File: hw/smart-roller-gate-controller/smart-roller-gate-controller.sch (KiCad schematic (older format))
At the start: 37 parts

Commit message: hw: sch complete, alpha version
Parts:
- R? (x2): value 10k -> 4.7k
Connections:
- net SCL is gone; now on net PZ_TX: DD?.36 (IO22)
- net SDA is gone; now on net PZ_RX: DD?.33 (IO21)
- net BLK1: now also DD?.12 (IO27)
- net BLK2: now also DD?.8 (IO32)
- net D_BUSY: now also DD?.6 (IO34)
- net D_DIN: now also DD?.16 (IO13); no longer DD?.14 (IO12)
- net GND: now also XP?.3 (Pin_3)
- net S2_ISR: now also DD?.7 (IO35)
- net ~RSNS: now also DD?.9 (IO33)
- net ~S2_RST: now also DD?.11 (IO26)
- net MOSI renamed MISO
- net MISO: now also DD?.14 (IO12); no longer DD?.16 (IO13)
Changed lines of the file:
@@
 Text GLabel 3800 2850 2    50   Output ~ 0
 ~RESET
-Text GLabel 3600 4250 2    50   Output ~ 0
+Text GLabel 3600 4250 2    50   UnSpc ~ 0
 ~RSNS
 Text GLabel 5050 2600 0    50   Input ~ 0
 ~RESET
-Text Notes 11300 7350 0    50   ~ 0
+Text Notes 11650 8650 0    50   ~ 0
 According to datasheet it is not necessary to pull-up/pull-down pins\n\nhttps://www.espressif.com/sites/default/files/documentation/esp32-wroom-32d_esp32-wroom-32u_datasheet_en.pdf
 $Comp
@@
 Wire Wire Line
 	13550 3850 13950 3850
+Text GLabel 13950 3750 2    50   Input ~ 0
+MISO
 Text GLabel 12400 3650 0    50   Input ~ 0
-MISO
-Text GLabel 13950 3750 2    50   Input ~ 0
 MOSI
 Text GLabel 13950 3650 2    50   Input ~ 0
@@
 P 5650 9300
 F 0 "R?" H 5720 9346 50  0000 L CNN
-F 1 "10k" H 5720 9255 50  0000 L CNN
+F 1 "4.7k" H 5720 9255 50  0000 L CNN
 F 2 "" V 5580 9300 50  0001 C CNN
 F 3 "~" H 5650 9300 50  0001 C CNN
@@
 P 5650 9400
 F 0 "R?" H 5720 9446 50  0000 L CNN
-F 1 "10k" H 5720 9355 50  0000 L CNN
+F 1 "4.7k" H 5720 9355 50  0000 L CNN
 F 2 "" V 5580 9400 50  0001 C CNN
 F 3 "~" H 5650 9400 50  0001 C CNN
@@
 Wire Wire Line
 	12500 2850 12400 2850
-Text GLabel 8850 6050 2    50   Input ~ 0
+Text GLabel 7600 4000 2    50   Output ~ 0
 PZ_RX
-Text GLabel 8900 6200 2    50   Output ~ 0
+Text GLabel 7600 4100 2    50   Input ~ 0
 PZ_TX
-Text GLabel 7600 4100 2    50   Input ~ 0
-SCL
-Text GLabel 7600 4000 2    50   Input ~ 0
-SDA
+Text GLabel 7600 4400 2    50   Input ~ 0
+~S2_RST
+Wire Wire Line
+	7000 4400 7600 4400
+Text GLabel 7150 4500 2    50   UnSpc ~ 0
+BLK1
+Text GLabel 7150 4600 2    50   UnSpc ~ 0
+BLK2
+Wire Wire Line
+	7000 4600 7150 4600
+Wire Wire Line
+	7150 4700 7000 4700
+Text GLabel 7150 4700 2    50   UnSpc ~ 0
+~RSNS
+Wire Wire Line
+	7000 4500 7150 4500
+Text GLabel 7550 4800 2    50   Input ~ 0
+D_BUSY
+Text GLabel 7550 4900 2    50   Input ~ 0
+S2_ISR
+Wire Wire Line
+	7000 4800 7550 4800
+Wire Wire Line
+	7000 4900 7550 4900
+Wire Wire Line
+	2900 4350 3200 4350
+Wire Wire Line
+	3200 4350 3200 4450
+Connection ~ 3200 4450
 $EndSCHEMATC

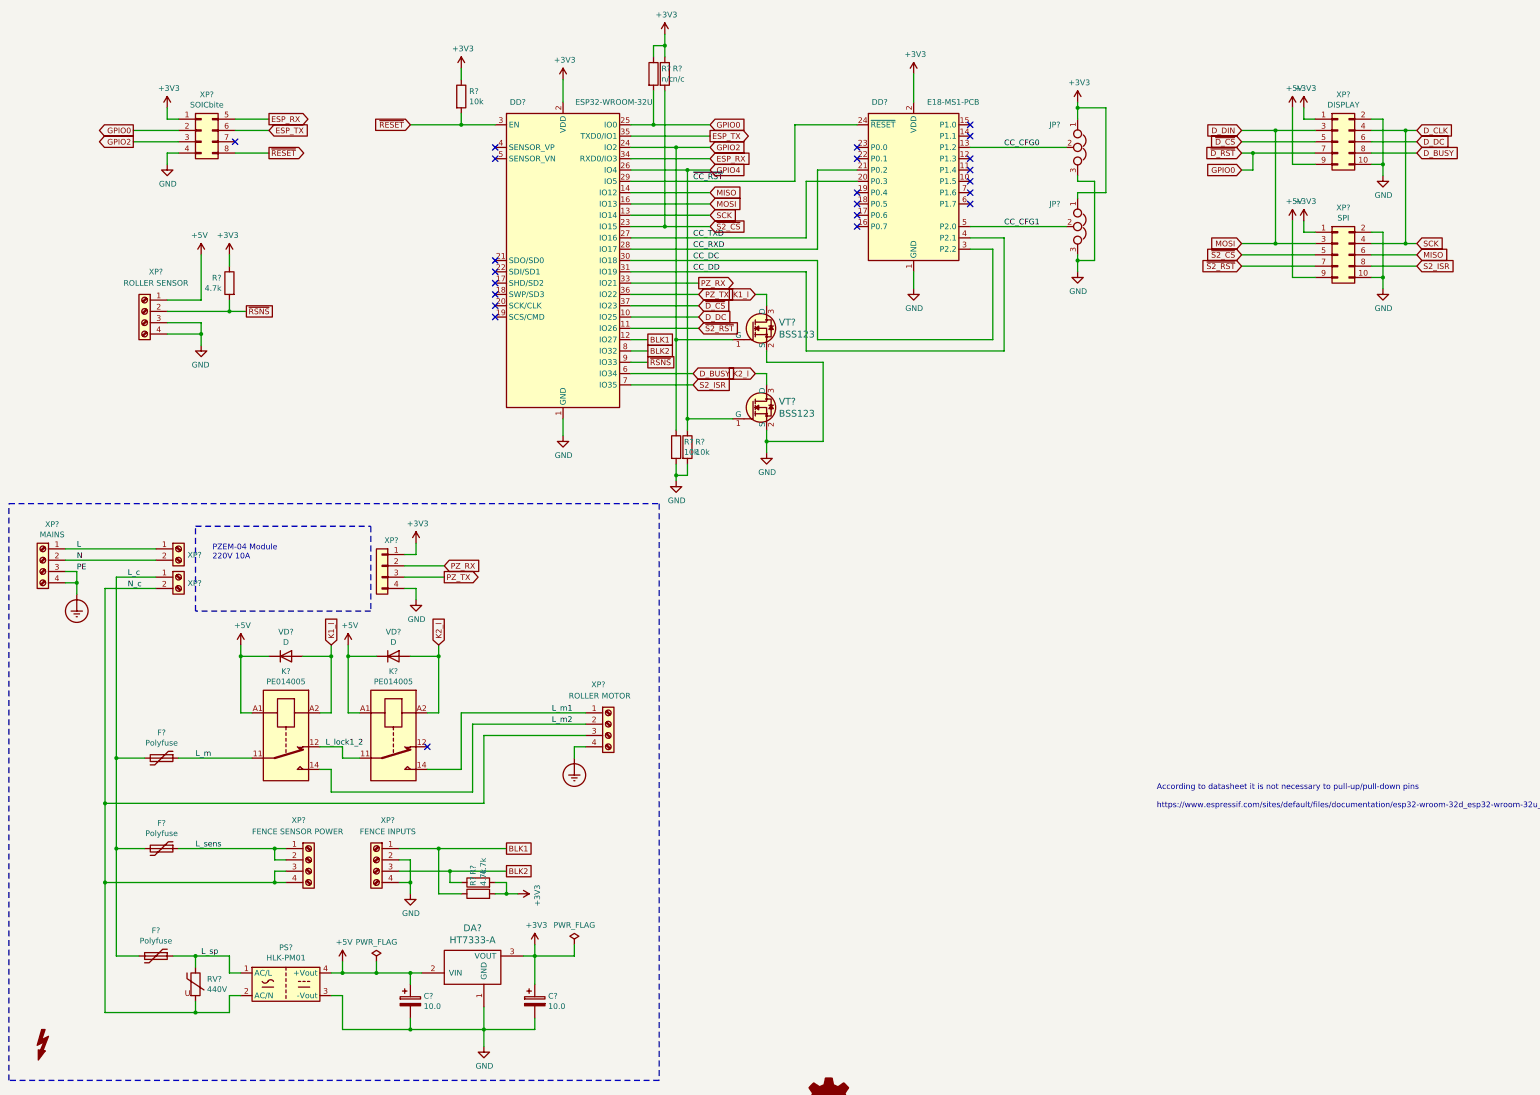
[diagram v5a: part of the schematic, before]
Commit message: hw: optimize pinout a bit
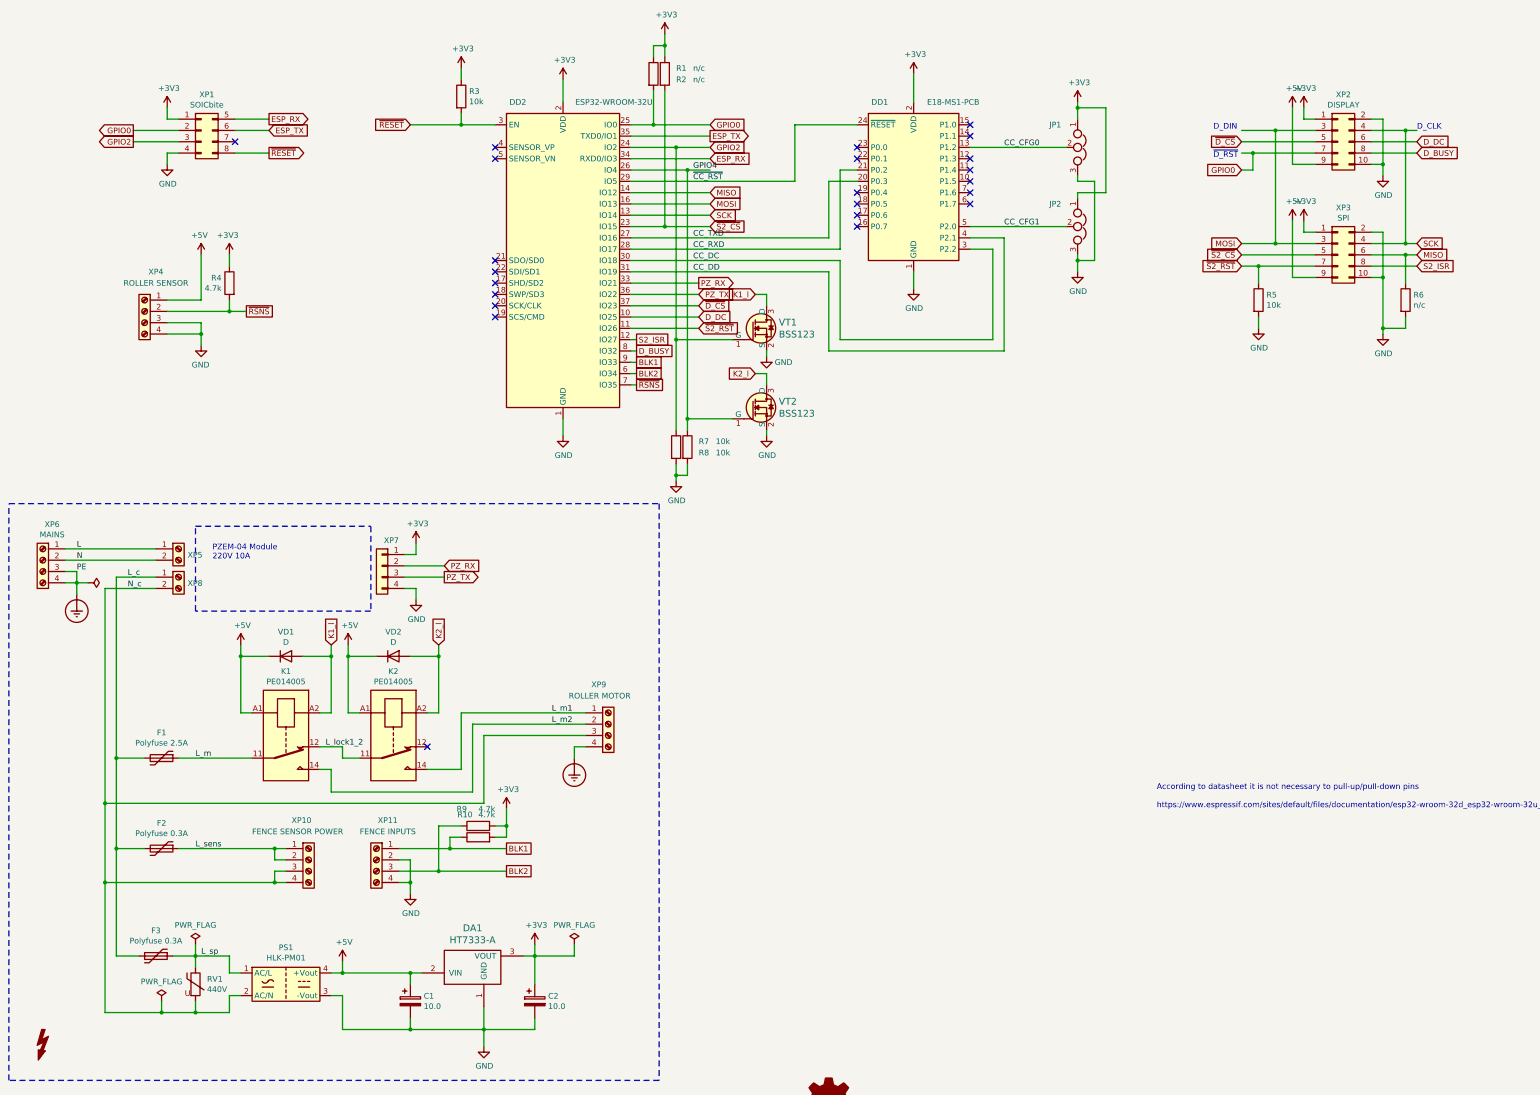
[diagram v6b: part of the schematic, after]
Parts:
- added R5: 10k, symbol Device:R
- added R6: n/c, symbol Device:R
- DA1: renamed from DA?; footprint (none) -> Package_TO_SOT_SMD:SOT-89-3
- F1: renamed from F?; value Polyfuse -> Polyfuse 2.5A
- F2, F3: renamed from F?; value Polyfuse -> Polyfuse 0.3A
- gave numbers to parts that had none: 33
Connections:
- net BLK1: now also DD2.9 (IO33); no longer DD2.12 (IO27)
- net BLK2: now also DD2.6 (IO34); no longer DD2.8 (IO32)
- net D_BUSY: now also DD2.8 (IO32); no longer DD2.6 (IO34)
- net GND: now also R5.2, R6.2
- net MISO: now also R6.1
- net S2_ISR: now also DD2.12 (IO27); no longer DD2.7 (IO35)
- net ~RSNS: now also DD2.7 (IO35); no longer DD2.9 (IO33)
- net ~S2_RST: now also R5.1
- net D_CLK renamed SCK
- net D_DIN renamed MOSI
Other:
- note added: "D_CLK"
- note added: "D_DIN"
- note added: "~D_RST"
- moved on the sheet: R10, R9

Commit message: hw: start routing
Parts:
- F1: footprint (none) -> Fuse:Fuse_Bourns_MF-RHT1300
- F2, F3: footprint (none) -> Fuse:Fuse_Bourns_MF-RHT200
- JP1, JP2: footprint (none) -> Jumper:SolderJumper-3_P1.3mm_Open_RoundedPad1.0x1.5mm
- R1, R10, R2, R3, R4, R5, R6, R7, R8, R9: footprint (none) -> Resistor_SMD:R_0603_1608Metric_Pad1.05x0.95mm_HandSolder
- RV1: footprint (none) -> Varistor:RV_Disc_D21.5mm_W4.9mm_P10mm
- VD1, VD2: footprint (none) -> Diode_SMD:D_SOD-123
- XP10, XP11, XP4, XP6, XP9: footprint (none) -> smart-roller-gate-controller:CONN-KF250-BA-4
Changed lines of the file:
@@
 F 0 "F3" V 2575 9950 50  0000 C CNN
 F 1 "Polyfuse 0.3A" V 2666 9950 50  0000 C CNN
-F 2 "" H 2850 9750 50  0001 L CNN
+F 2 "Fuse:Fuse_Bourns_MF-RHT200" H 2850 9750 50  0001 L CNN
 F 3 "~" H 2800 9950 50  0001 C CNN
 	1    2800 9950
@@
 F 0 "JP1" V 10750 2550 50  0000 L CNN
 F 1 "Jumper_NC_Dual" V 10995 2902 50  0001 L CNN
-F 2 "" H 10950 2800 50  0001 C CNN
+F 2 "Jumper:SolderJumper-3_P1.3mm_Open_RoundedPad1.0x1.5mm" H 10950 2800 50  0001 C CNN
 F 3 "~" H 10950 2800 50  0001 C CNN
 	1    10950 2800
@@
 F 0 "JP2" V 10750 3250 50  0000 L CNN
 F 1 "Jumper_NC_Dual" V 11050 3800 50  0001 L CNN
-F 2 "" H 10950 3500 50  0001 C CNN
+F 2 "Jumper:SolderJumper-3_P1.3mm_Open_RoundedPad1.0x1.5mm" H 10950 3500 50  0001 C CNN
 F 3 "~" H 10950 3500 50  0001 C CNN
 	1    10950 3500
@@
 F 0 "RV1" H 3252 10246 50  0000 L CNN
 F 1 "440V" H 3252 10155 50  0000 L CNN
-F 2 "" V 3080 10200 50  0001 C CNN
+F 2 "Varistor:RV_Disc_D21.5mm_W4.9mm_P10mm" V 3080 10200 50  0001 C CNN
 F 3 "~" H 3150 10200 50  0001 C CNN
 	1    3150 10200
@@
 F 0 "XP6" H 1718 6767 50  0000 C CNN
 F 1 "MAINS" H 1718 6676 50  0000 C CNN
-F 2 "" H 1800 6450 50  0001 C CNN
+F 2 "smart-roller-gate-controller:CONN-KF250-BA-4" H 1800 6450 50  0001 C CNN
 F 3 "~" H 1800 6450 50  0001 C CNN
 	1    1800 6450
@@
 F 0 "F2" V 2625 9000 50  0000 C CNN
 F 1 "Polyfuse 0.3A" V 2716 9000 50  0000 C CNN
-F 2 "" H 2900 8800 50  0001 L CNN
+F 2 "Fuse:Fuse_Bourns_MF-RHT200" H 2900 8800 50  0001 L CNN
 F 3 "~" H 2850 9000 50  0001 C CNN
 	1    2850 9000
@@
 F 0 "XP10" H 4000 9450 50  0000 L CNN
 F 1 "FENCE SENSOR POWER" H 3650 9350 50  0000 L CNN
-F 2 "" H 4150 9100 50  0001 C CNN
+F 2 "smart-roller-gate-controller:CONN-KF250-BA-4" H 4150 9100 50  0001 C CNN
 F 3 "~" H 4150 9100 50  0001 C CNN
 	1    4150 9100
@@
 F 0 "XP9" H 6650 8250 50  0000 L CNN
 F 1 "ROLLER MOTOR" H 6450 8150 50  0000 L CNN
-F 2 "" H 6800 7900 50  0001 C CNN
+F 2 "smart-roller-gate-controller:CONN-KF250-BA-4" H 6800 7900 50  0001 C CNN
 F 3 "~" H 6800 7900 50  0001 C CNN
 	1    6800 7900
@@
 F 0 "XP11" H 4650 9450 50  0000 C CNN
 F 1 "FENCE INPUTS" H 4650 9350 50  0000 C CNN
-F 2 "" H 4750 9100 50  0001 C CNN
+F 2 "smart-roller-gate-controller:CONN-KF250-BA-4" H 4750 9100 50  0001 C CNN
 F 3 "~" H 4750 9100 50  0001 C CNN
 	1    4750 9100
@@
 F 0 "XP4" H 2600 4600 50  0000 C CNN
 F 1 "ROLLER SENSOR" H 2600 4500 50  0000 C CNN
-F 2 "" H 2700 4250 50  0001 C CNN
+F 2 "smart-roller-gate-controller:CONN-KF250-BA-4" H 2700 4250 50  0001 C CNN
 F 3 "~" H 2700 4250 50  0001 C CNN
 	1    2700 4250
@@
 F 0 "R3" H 5570 2396 50  0000 L CNN
 F 1 "10k" H 5570 2305 50  0000 L CNN
-F 2 "" V 5430 2350 50  0001 C CNN
+F 2 "Resistor_SMD:R_0603_1608Metric_Pad1.05x0.95mm_HandSolder" V 5430 2350 50  0001 C CNN
 F 3 "~" H 5500 2350 50  0001 C CNN
 	1    5500 2350
@@
 F 0 "F1" V 2625 8200 50  0000 C CNN
 F 1 "Polyfuse 2.5A" V 2716 8200 50  0000 C CNN
-F 2 "" H 2900 8000 50  0001 L CNN
+F 2 "Fuse:Fuse_Bourns_MF-RHT1300" H 2900 8000 50  0001 L CNN
 F 3 "~" H 2850 8200 50  0001 C CNN
 	1    2850 8200
@@
 F 0 "VD1" H 3950 7516 50  0000 C CNN
 F 1 "D" H 3950 7425 50  0000 C CNN
-F 2 "" H 3950 7300 50  0001 C CNN
+F 2 "Diode_SMD:D_SOD-123" H 3950 7300 50  0001 C CNN
 F 3 "~" H 3950 7300 50  0001 C CNN
 	1    3950 7300
@@
 F 0 "VD2" H 4900 7516 50  0000 C CNN
 F 1 "D" H 4900 7425 50  0000 C CNN
-F 2 "" H 4900 7300 50  0001 C CNN
+F 2 "Diode_SMD:D_SOD-123" H 4900 7300 50  0001 C CNN
 F 3 "~" H 4900 7300 50  0001 C CNN
 	1    4900 7300
@@
 F 0 "R4" H 3520 4046 50  0000 L CNN
 F 1 "4.7k" H 3520 3955 50  0000 L CNN
-F 2 "" V 3380 4000 50  0001 C CNN
+F 2 "Resistor_SMD:R_0603_1608Metric_Pad1.05x0.95mm_HandSolder" V 3380 4000 50  0001 C CNN
 F 3 "~" H 3450 4000 50  0001 C CNN
 	1    3450 4000
@@
 F 0 "R1" H 7400 2200 50  0000 L CNN
 F 1 "n/c" H 7550 2200 50  0000 L CNN
-F 2 "" V 7130 2150 50  0001 C CNN
+F 2 "Resistor_SMD:R_0603_1608Metric_Pad1.05x0.95mm_HandSolder" V 7130 2150 50  0001 C CNN
 F 3 "~" H 7200 2150 50  0001 C CNN
 	1    7200 2150
@@
 F 0 "R2" H 7400 2100 50  0000 L CNN
 F 1 "n/c" H 7550 2100 50  0000 L CNN
-F 2 "" V 7230 2150 50  0001 C CNN
+F 2 "Resistor_SMD:R_0603_1608Metric_Pad1.05x0.95mm_HandSolder" V 7230 2150 50  0001 C CNN
 F 3 "~" H 7300 2150 50  0001 C CNN
 	1    7300 2150
@@
 F 0 "R7" H 7600 5500 50  0000 L CNN
 F 1 "10k" H 7750 5500 50  0000 L CNN
-F 2 "" V 7330 5450 50  0001 C CNN
+F 2 "Resistor_SMD:R_0603_1608Metric_Pad1.05x0.95mm_HandSolder" V 7330 5450 50  0001 C CNN
 F 3 "~" H 7400 5450 50  0001 C CNN
 	1    7400 5450
@@
 F 0 "R8" H 7600 5400 50  0000 L CNN
 F 1 "10k" H 7750 5400 50  0000 L CNN
-F 2 "" V 7430 5450 50  0001 C CNN
+F 2 "Resistor_SMD:R_0603_1608Metric_Pad1.05x0.95mm_HandSolder" V 7430 5450 50  0001 C CNN
 F 3 "~" H 7500 5450 50  0001 C CNN
 	1    7500 5450
@@
 F 0 "R9" V 5800 8900 50  0000 L CNN
 F 1 "4.7k" V 5800 8650 50  0000 L CNN
-F 2 "" V 5580 8800 50  0001 C CNN
+F 2 "Resistor_SMD:R_0603_1608Metric_Pad1.05x0.95mm_HandSolder" V 5580 8800 50  0001 C CNN
 F 3 "~" H 5650 8800 50  0001 C CNN
 	1    5650 8800
@@
 F 0 "R10" V 5850 8950 50  0000 L CNN
 F 1 "4.7k" V 5850 8750 50  0000 L CNN
-F 2 "" V 5580 8900 50  0001 C CNN
+F 2 "Resistor_SMD:R_0603_1608Metric_Pad1.05x0.95mm_HandSolder" V 5580 8900 50  0001 C CNN
 F 3 "~" H 5650 8900 50  0001 C CNN
 	1    5650 8900
@@
 F 0 "R5" H 12620 4196 50  0000 L CNN
 F 1 "10k" H 12620 4105 50  0000 L CNN
-F 2 "" V 12480 4150 50  0001 C CNN
+F 2 "Resistor_SMD:R_0603_1608Metric_Pad1.05x0.95mm_HandSolder" V 12480 4150 50  0001 C CNN
 F 3 "~" H 12550 4150 50  0001 C CNN
 	1    12550 4150
@@
 F 0 "R6" H 13920 4196 50  0000 L CNN
 F 1 "n/c" H 13920 4105 50  0000 L CNN
-F 2 "" V 13780 4150 50  0001 C CNN
+F 2 "Resistor_SMD:R_0603_1608Metric_Pad1.05x0.95mm_HandSolder" V 13780 4150 50  0001 C CNN
 F 3 "~" H 13850 4150 50  0001 C CNN
 	1    13850 4150

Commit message: hw: initial placement
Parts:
- removed XP5, XP8: Screw_Terminal_01x02, Connector_Wire:SolderWirePad_1x02_P5.08mm_Drill1.5mm, symbol Connector:Screw_Terminal_01x02
- added J1: L, Connector_Wire:SolderWirePad_1x01_Drill1.2mm, symbol Connector:Conn_01x01_Female
- added J2: N, Connector_Wire:SolderWirePad_1x01_Drill1.2mm, symbol Connector:Conn_01x01_Female
- added J3: L_c, Connector_Wire:SolderWirePad_1x01_Drill1.2mm, symbol Connector:Conn_01x01_Female
- added J4: N_c, Connector_Wire:SolderWirePad_1x01_Drill1.2mm, symbol Connector:Conn_01x01_Female
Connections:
- net L: now also J1.1 (Pin_1)
- net L_c: now also J3.1 (Pin_1)
- net N: now also J2.1 (Pin_1)
- net N_c: now also J4.1 (Pin_1)
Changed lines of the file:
@@
 Text Notes 3300 6450 0    50   ~ 0
 PZEM-04 Module\n220V 10A
-$Comp
-L Connector:Screw_Terminal_01x02 XP5
-U 1 1 5E2FD226
-P 3000 6350
-F 0 "XP5" H 3080 6296 50  0000 L CNN
-F 1 "Screw_Terminal_01x02" H 3080 6251 50  0001 L CNN
-F 2 "Connector_Wire:SolderWirePad_1x02_P5.08mm_Drill1.5mm" H 3000 6350 50  0001 C CNN
-F 3 "~" H 3000 6350 50  0001 C CNN
-	1    3000 6350
-	1    0    0    -1
-$EndComp
-$Comp
-L Connector:Screw_Terminal_01x02 XP8
-U 1 1 5E2FDA9D
-P 3000 6600
-F 0 "XP8" H 3080 6546 50  0000 L CNN
-F 1 "Screw_Terminal_01x02" H 3080 6501 50  0001 L CNN
-F 2 "Connector_Wire:SolderWirePad_1x02_P5.08mm_Drill1.5mm" H 3000 6600 50  0001 C CNN
-F 3 "~" H 3000 6600 50  0001 C CNN
-	1    3000 6600
-	1    0    0    -1
-$EndComp
 Wire Wire Line
 	2000 6350 2800 6350
@@
 Wire Wire Line
 	8200 4600 8200 4650
+$Comp
+L Connector:Conn_01x01_Female J3
+U 1 1 5EDF2DCE
+P 3000 6600
+F 0 "J3" H 3050 6600 50  0000 L CNN
+F 1 "L_c" H 3150 6600 50  0000 L CNN
+F 2 "Connector_Wire:SolderWirePad_1x01_Drill1.2mm" H 3000 6600 50  0001 C CNN
+F 3 "~" H 3000 6600 50  0001 C CNN
+	1    3000 6600
+	1    0    0    -1
+$EndComp
+$Comp
+L Connector:Conn_01x01_Female J4
+U 1 1 5EDF3216
+P 3000 6700
+F 0 "J4" H 3050 6700 50  0000 L CNN
+F 1 "N_c" H 3150 6700 50  0000 L CNN
+F 2 "Connector_Wire:SolderWirePad_1x01_Drill1.2mm" H 3000 6700 50  0001 C CNN
+F 3 "~" H 3000 6700 50  0001 C CNN
+	1    3000 6700
+	1    0    0    -1
+$EndComp
+$Comp
+L Connector:Conn_01x01_Female J1
+U 1 1 5EDF5A1B
+P 3000 6350
+F 0 "J1" H 3050 6350 50  0000 L CNN
+F 1 "L" H 3150 6350 50  0000 L CNN
+F 2 "Connector_Wire:SolderWirePad_1x01_Drill1.2mm" H 3000 6350 50  0001 C CNN
+F 3 "~" H 3000 6350 50  0001 C CNN
+	1    3000 6350
+	1    0    0    -1
+$EndComp
+$Comp
+L Connector:Conn_01x01_Female J2
+U 1 1 5EDF5D02
+P 3000 6450
+F 0 "J2" H 3050 6450 50  0000 L CNN
+F 1 "N" H 3150 6450 50  0000 L CNN
+F 2 "Connector_Wire:SolderWirePad_1x01_Drill1.2mm" H 3000 6450 50  0001 C CNN
+F 3 "~" H 3000 6450 50  0001 C CNN
+	1    3000 6450
+	1    0    0    -1
+$EndComp
 $EndSCHEMATC
